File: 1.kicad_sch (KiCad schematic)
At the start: 1 part, among them J1 ERF8-025-05.0-L-DV-L-K-TR

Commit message: initialized for 4-card
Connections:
- net SPI1.MISO is gone; now on net 5V0_USB: J1.32
- net SPI1.MOSI is gone; now on net GND: J1.30
- net SPI1.SCLK is gone; now on net 5V0_USB: J1.38
- net USB3.TX_N is gone; now on net GND: J1.22
- net USB3.TX_P is gone; now on net GND: J1.24
- net GND: now also J1.25, J1.27; no longer J1.31, J1.34, J1.36, J1.37, J1.39, J1.42, J1.44, J1.50
- net 5V0_3: now reaches J1.33
- net 5V0_3: now also J1.31, J1.35, J1.37, J1.39
- net 5V0_2: now reaches J1.46
- net 5V0_2: now also J1.42, J1.44, J1.48, J1.50
- net 5V0 renamed 5V0_1
- net SPI1.CS0n renamed 5V0_USB
- net 5V0_USB: now also J1.34, J1.36
- net USB3.D_N: no longer names the net of J1.6
- net USB3.D_P: no longer names the net of J1.8
- net USB3.RX_N: no longer names the net of J1.14
- net USB3.RX_P: no longer names the net of J1.16

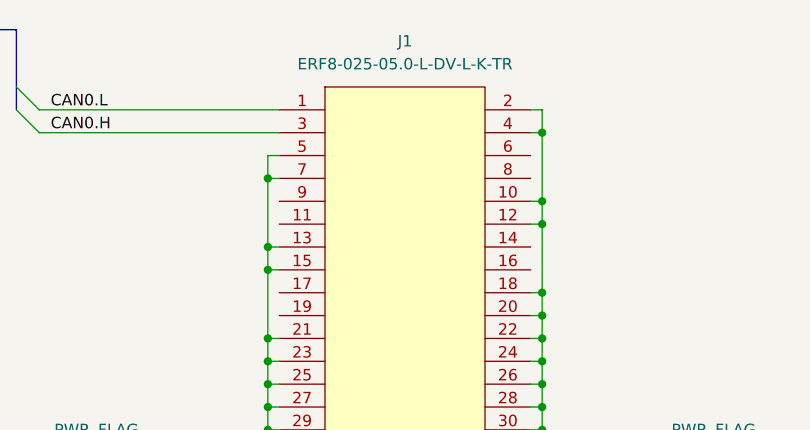
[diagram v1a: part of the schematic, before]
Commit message: fixed footprint link
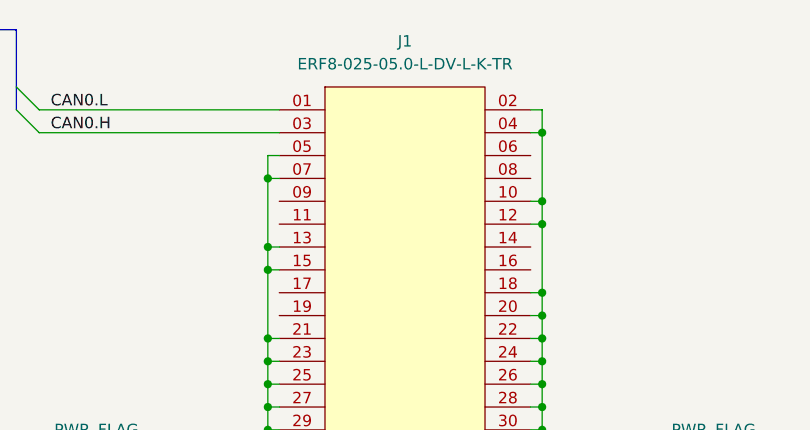
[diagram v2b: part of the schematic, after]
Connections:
- net CAN0.H: now also J1.03; no longer J1.3
- net CAN0.L: now also J1.01; no longer J1.1
- net GND: now also J1.02, J1.04, J1.05, J1.07; no longer J1.2, J1.4, J1.5, J1.7
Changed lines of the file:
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@@
 		(pin "10"
 		)
-		(pin "8"
-		)
-		(pin "6"
-		)
-		(pin "4"
-		)
-		(pin "2"
+		(pin "01"
+		)
+		(pin "03"
+		)
+		(pin "05"
+		)
+		(pin "07"
 		)
 		(pin "40"
@@
 		(pin "11"
 		)
-		(pin "9"
-		)
-		(pin "7"
-		)
-		(pin "5"
-		)
-		(pin "3"
-		)
-		(pin "1"
+		(pin "09"
+		)
+		(pin "02"
+		)
+		(pin "04"
+		)
+		(pin "06"
+		)
+		(pin "08"
 		)
 		(pin "33"
@@
 		(dnp no)
 		(fields_autoplaced yes)
-		(property "Reference" "#PWR?"
+		(property "Reference" "#PWR0101"
 			(at 157.48 140.97 0)
 			(effects
@@
 			(project "CUTIE-BACKPLANE"
 				(path "/db751f7b-eeef-4f9a-a021-6b6484a5d83e/5d57494b-e2eb-4102-8e3d-493d9414839f"
-					(reference "#PWR?")
+					(reference "#PWR0101")
 					(unit 1)
 				)
@@
 		(dnp no)
 		(fields_autoplaced yes)
-		(property "Reference" "#PWR?"
+		(property "Reference" "#PWR0102"
 			(at 127 140.97 0)
 			(effects
@@
 			(project "CUTIE-BACKPLANE"
 				(path "/db751f7b-eeef-4f9a-a021-6b6484a5d83e/5d57494b-e2eb-4102-8e3d-493d9414839f"
-					(reference "#PWR?")
+					(reference "#PWR0102")
 					(unit 1)
 				)

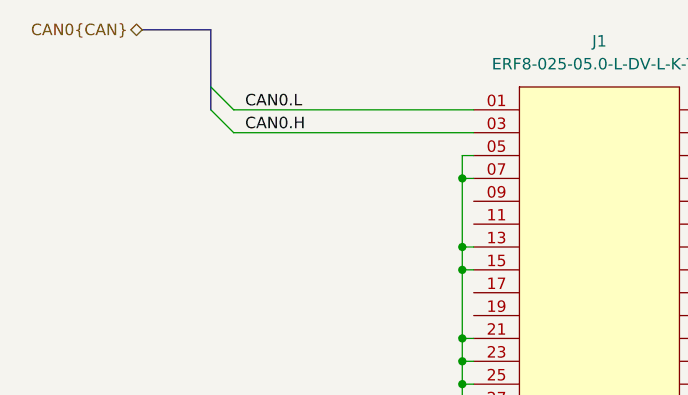
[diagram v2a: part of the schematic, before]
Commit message: added pwr leds and edge cuts
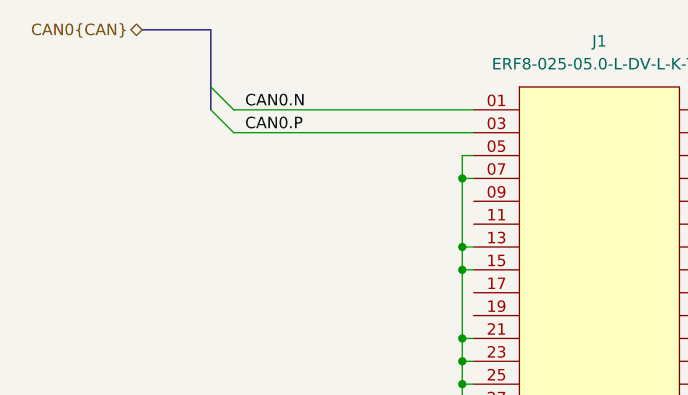
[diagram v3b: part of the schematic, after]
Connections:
- net CAN0.H renamed CAN0.P
- net CAN0.L renamed CAN0.N
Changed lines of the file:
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@@
 		)
 	)
-	(label "CAN0.H"
+	(label "CAN0.P"
 		(at 102.87 71.12 0)
 		(effects
@@
 		)
 	)
-	(label "CAN0.L"
+	(label "CAN0.N"
 		(at 102.87 68.58 0)
 		(effects

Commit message: prelim layout complete
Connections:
- net 5V0_1: now also J1.02, J1.04, J1.06, J1.08, J1.10; no longer J1.41, J1.43, J1.45, J1.47, J1.49
- net 5V0_2: now also J1.01, J1.03, J1.05, J1.07, J1.09; no longer J1.42, J1.44, J1.46, J1.48, J1.50
- net 5V0_3: now also J1.12, J1.14, J1.16, J1.18, J1.20; no longer J1.31, J1.33, J1.35, J1.37, J1.39
- net 5V0_USB: now also J1.11, J1.13, J1.15, J1.17, J1.19; no longer J1.32, J1.34, J1.36, J1.38, J1.40
- net CAN0.N: now also J1.50; no longer J1.01
- net CAN0.P: now also J1.48; no longer J1.03
- net GND: now also J1.31, J1.33, J1.36, J1.38, J1.39, J1.41, J1.44, J1.46, J1.47, J1.49; no longer J1.02, J1.04, J1.05, J1.07, J1.10, J1.12, J1.13, J1.15, J1.18, J1.20
